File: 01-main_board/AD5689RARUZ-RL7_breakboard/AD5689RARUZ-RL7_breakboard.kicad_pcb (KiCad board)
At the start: 2 copper layers, 37.5 x 24 mm, 7 parts, among them J1 Conn_01x06, J2 Conn_01x08, U1 AD5689RARUZ-RL7

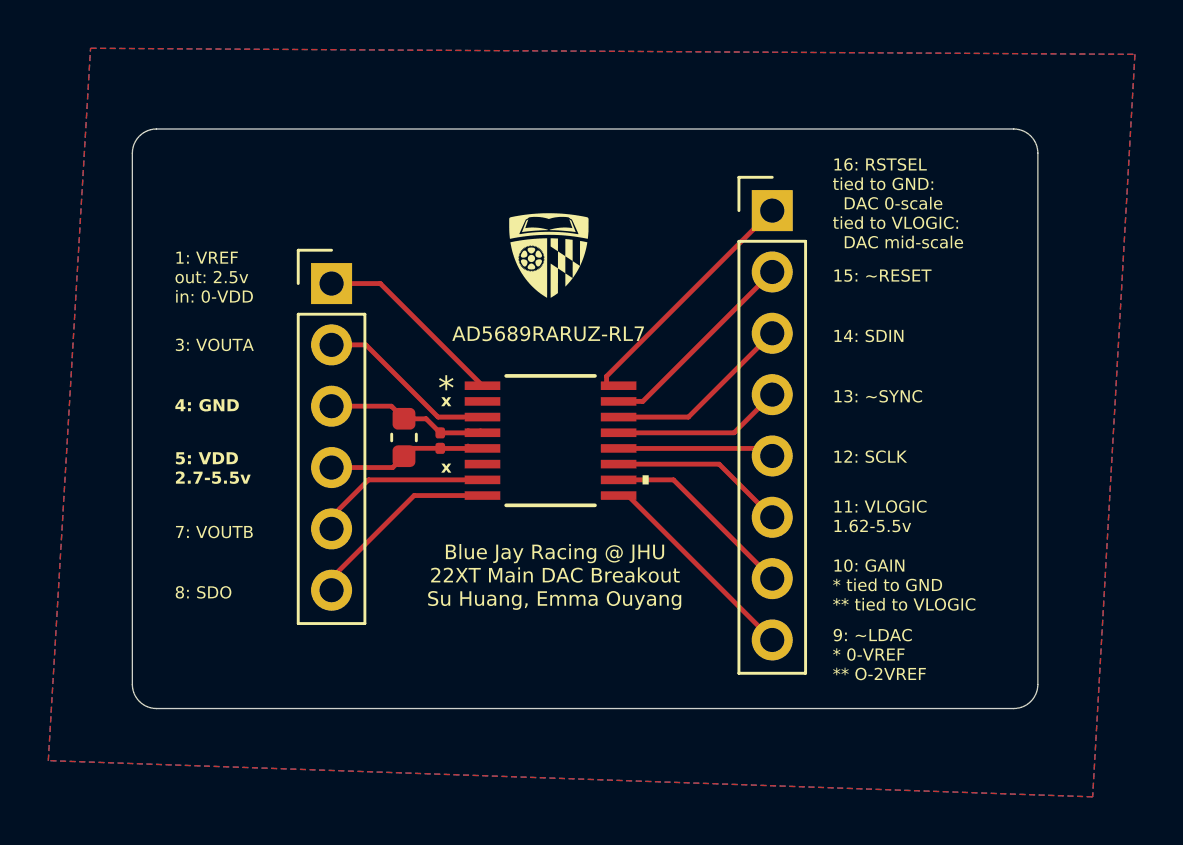
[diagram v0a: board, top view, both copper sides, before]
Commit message: updated breakout size
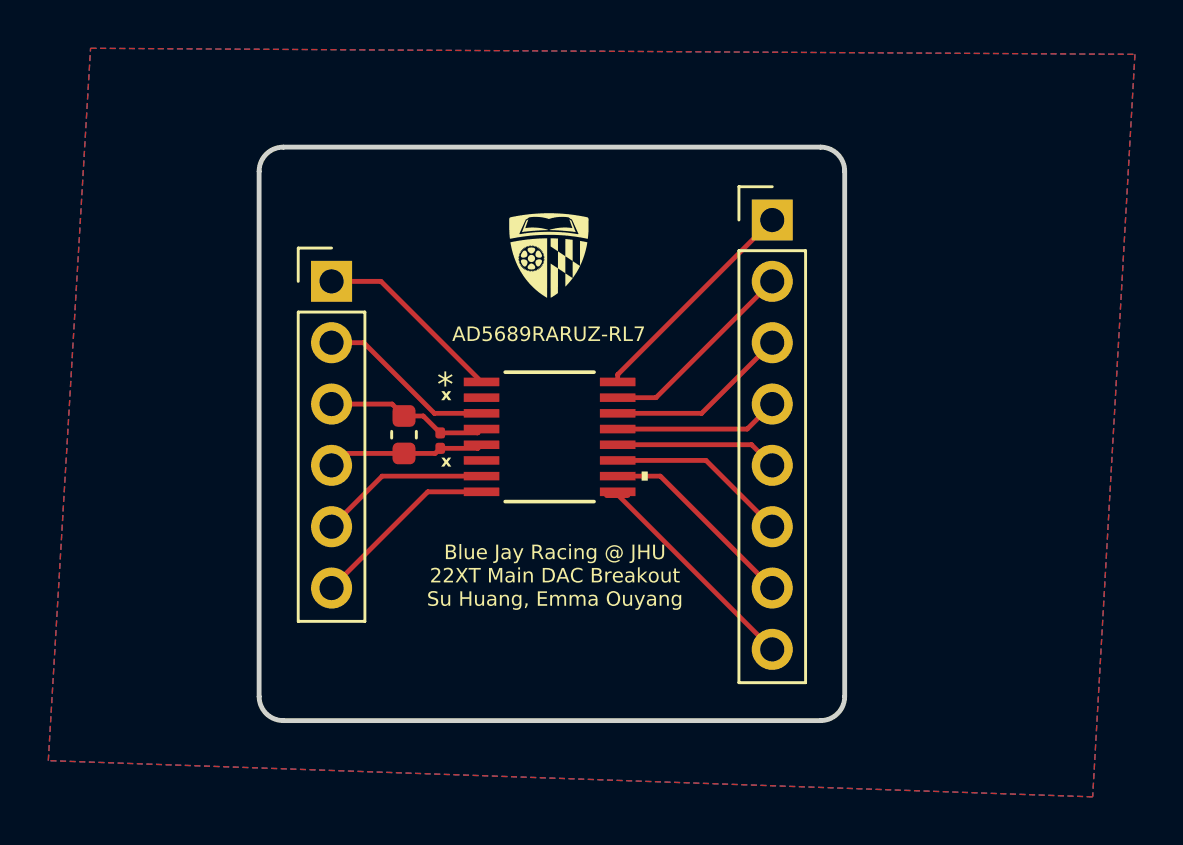
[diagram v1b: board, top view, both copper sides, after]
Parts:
- removed the G*** at (144.8, 66.2)
- moved J2 0.39 mm to (154.0, 64.8)
- moved U1 0.16 mm to (144.8, 73.8)
- moved C1 0.12 mm to (138.8, 73.7)
- moved J1 0.09 mm to (135.8, 67.3)
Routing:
- net RSTSEL: track 10.1 -> 9.36 mm
- net *LDAC: track 9.34 -> 10.1 mm
- net GND: track 7.46 -> 6.77 mm
- net SDIN: track 8.30 -> 7.61 mm
- net *RESET: track 9.08 -> 8.40 mm
- net *SYNC: track 7.52 -> 6.83 mm
- net VOUTA: track 7.99 -> 7.42 mm
- net VREF: track 8.50 -> 7.94 mm
- net VOUTB: track 7.59 -> 7.08 mm
- net SDO: track 8.37 -> 7.86 mm
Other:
- board size 37.5 x 24 mm -> 24.2 x 23.8 mm

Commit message: Checked and added via stitching
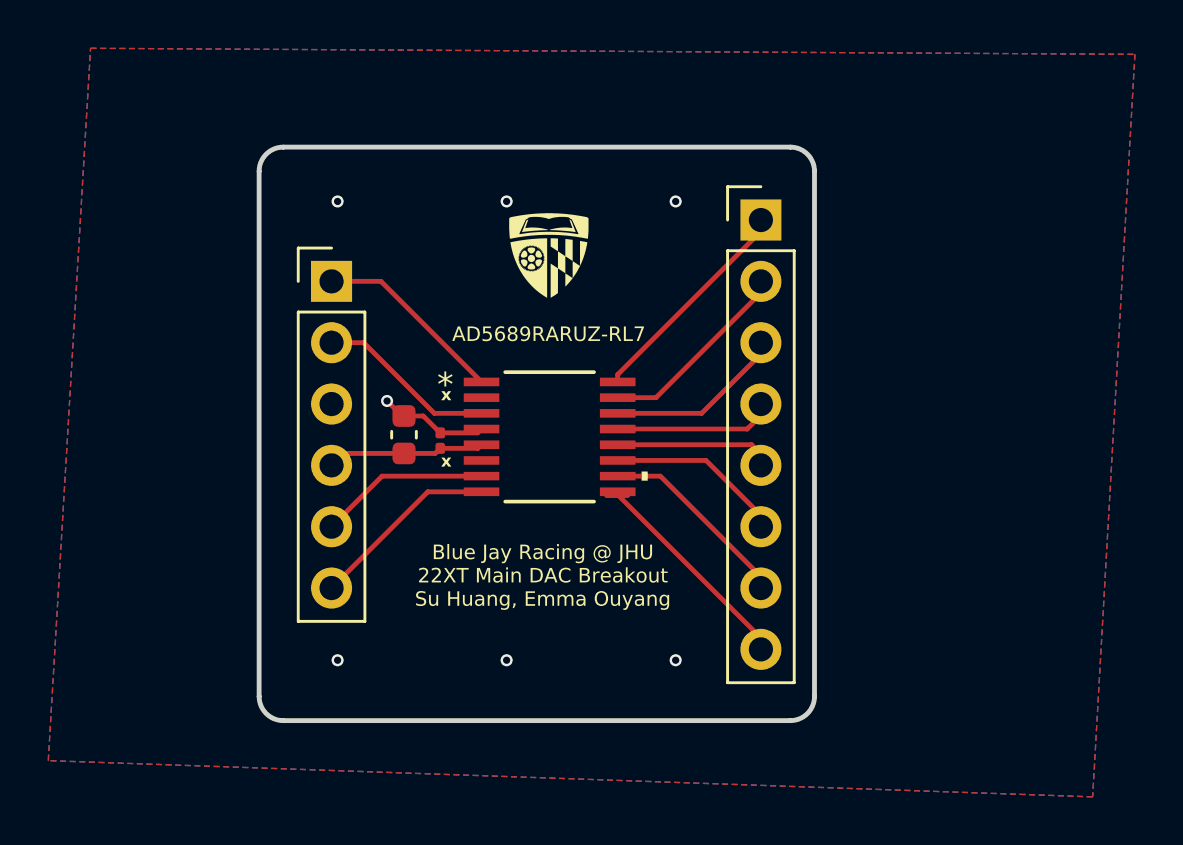
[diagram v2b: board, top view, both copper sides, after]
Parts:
- moved J2 0.47 mm to (153.5, 64.8)
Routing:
- net GND: track 6.77 -> 4.53 mm, vias 0 -> 7
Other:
- board size 24.2 x 23.8 mm -> 23 x 23.8 mm
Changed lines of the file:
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@@
 			(sketchdnponfab yes)
 			(crossoutdnponfab yes)
-			(subtractmaskfromsilk no)
+			(subtractmaskfromsilk yes)
 			(outputformat 1)
 			(mirror no)
@@
 	(footprint "Connector_PinHeader_2.54mm:PinHeader_1x08_P2.54mm_Vertical"
 		(layer "F.Cu")
-		(at 154 64.77)
+		(at 153.53 64.77)
 		(descr "Through hole straight pin header, 1x08, 2.54mm pitch, single row")
 		(tags "Through hole pin header THT 1x08 2.54mm single row")
@@
 		(model "${KICAD9_3DMODEL_DIR}/Connector_PinHeader_2.54mm.3dshapes/PinHeader_1x08_P2.54mm_Vertical.step"
 			(offset
-				(xyz 0 0 0)
+				(xyz 0 0 -1.5)
 			)
 			(scale
@@
 		(model "${KICAD9_3DMODEL_DIR}/Connector_PinHeader_2.54mm.3dshapes/PinHeader_1x06_P2.54mm_Vertical.step"
 			(offset
-				(xyz 0 0 0)
+				(xyz 0 0 -1.5)
 			)
 			(scale
@@
 	)
 	(gr_arc
-		(start 157 84.5)
-		(mid 156.707107 85.207107)
-		(end 156 85.5)
+		(start 155.75 84.5)
+		(mid 155.457107 85.207107)
+		(end 154.75 85.5)
 		(stroke
 			(width 0.2)
@@
 	)
 	(gr_line
-		(start 157 62.75)
-		(end 157 84.5)
+		(start 155.75 62.75)
+		(end 155.75 84.5)
 		(stroke
 			(width 0.2)
@@
 	(gr_line
 		(start 133.75 61.75)
-		(end 156 61.75)
+		(end 154.75 61.75)
 		(stroke
 			(width 0.2)
-			(type default)
+			(type solid)
 		)
 		(layer "Edge.Cuts")
 	)
 	(gr_line
-		(start 156 85.5)
-		(end 133.75 85.5)
+		(start 133.75 85.5)
+		(end 154.75 85.5)
 		(stroke
 			(width 0.2)
-			(type default)
+			(type solid)
 		)
 		(layer "Edge.Cuts")
 	)
 	(gr_arc
-		(start 156 61.75)
-		(mid 156.707107 62.042893)
-		(end 157 62.75)
+		(start 154.75 61.75)
+		(mid 155.457107 62.042893)
+		(end 155.75 62.75)
 		(stroke
 			(width 0.2)
@@
 	)
 	(gr_text "Blue Jay Racing @ JHU\n22XT Main DAC Breakout\nSu Huang, Emma Ouyang"
-		(at 145 79.5 0)
+		(at 144.5 79.5 0)
 		(layer "F.SilkS")
 		(effects
@@
 		)
 	)
+	(dimension
+		(type orthogonal)
+		(layer "Cmts.User")
+		(pts
+			(xy 135.75 81.28) (xy 153.543 81.28)
+		)
+		(height 11.303)
+		(orientation 0)
+		(format
+			(prefix "")
+			(suffix "")
+			(units 0)
+			(units_format 0)
+			(precision 4)
+			(suppress_zeroes yes)
+		)
+		(style
+			(thickness 0.2)
+			(arrow_length 1.27)
+			(text_position_mode 0)
+			(arrow_direction outward)
+			(extension_height 0.58642)
+			(extension_offset 0.5)
+			(keep_text_aligned yes)
+		)
+		(gr_text "0.7005"
+			(at 144.6465 90.783 0)
+			(layer "Cmts.User")
+			(effects
+				(font
+					(size 1.5 1.5)
+					(thickness 0.3)
+				)
+			)
+		)
+	)
 	(segment
 		(start 139.55 72.885)
@@
 	)
 	(segment
-		(start 135.75 72.39)
-		(end 138.255 72.39)
+		(start 138.75 72.885)
+		(end 138.671 72.885)
 		(width 0.2)
 		(layer "F.Cu")
@@
 	)
 	(segment
-		(start 138.255 72.39)
-		(end 138.75 72.885)
+		(start 138.671 72.885)
+		(end 138.049 72.263)
 		(width 0.2)
 		(layer "F.Cu")
@@
 		(net 1)
 	)
+	(via
+		(at 136 83)
+		(size 0.5)
+		(drill 0.3)
+		(layers "F.Cu" "B.Cu")
+		(net 1)
+	)
+	(via
+		(at 143 83)
+		(size 0.5)
+		(drill 0.3)
+		(layers "F.Cu" "B.Cu")
+		(net 1)
+	)
+	(via
+		(at 143 64)
+		(size 0.5)
+		(drill 0.3)
+		(layers "F.Cu" "B.Cu")
+		(net 1)
+	)
+	(via
+		(at 136 64)
+		(size 0.5)
+		(drill 0.3)
+		(layers "F.Cu" "B.Cu")
+		(net 1)
+	)
+	(via
+		(at 138.049 72.263)
+		(size 0.5)
+		(drill 0.3)
+		(layers "F.Cu" "B.Cu")
+		(net 1)
+	)
+	(via
+		(at 150 83)
+		(size 0.5)
+		(drill 0.3)
+		(layers "F.Cu" "B.Cu")
+		(net 1)
+	)
+	(via
+		(at 150 64)
+		(size 0.5)
+		(drill 0.3)
+		(layers "F.Cu" "B.Cu")
+		(net 1)
+	)
 	(segment
 		(start 140.25 74.225)
@@
 	)
 	(zone
+		(net 0)
+		(net_name "")
+		(layer "F.Cu")
+		(name "Keepout")
+		(hatch edge 0.5)
+		(connect_pads
+			(clearance 0)
+		)
+		(min_thickness 0.25)
+		(filled_areas_thickness no)
+		(keepout
+			(tracks allowed)
+			(vias allowed)
+			(pads allowed)
+			(copperpour not_allowed)
+			(footprints allowed)
+		)
+		(placement
+			(enabled no)
+			(sheetname "")
+		)
+		(fill
+			(thermal_gap 0.5)
+			(thermal_bridge_width 0.5)
+		)
+		(polygon
+			(pts
+				(xy 139.319 74.549) (xy 140.966539 74.549) (xy 140.966539 75.184) (xy 139.192 75.184) (xy 139.192 74.672185)
+				(xy 139.319 74.545185)
+			)
+		)
+	)
+	(zone

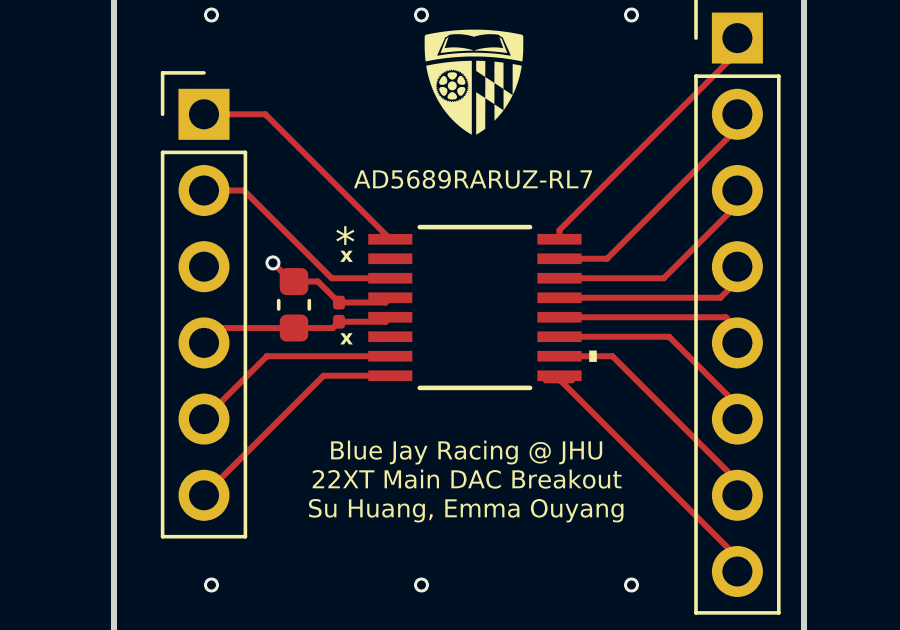
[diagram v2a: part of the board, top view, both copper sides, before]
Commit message: changed 0201 to 0402 capacitor
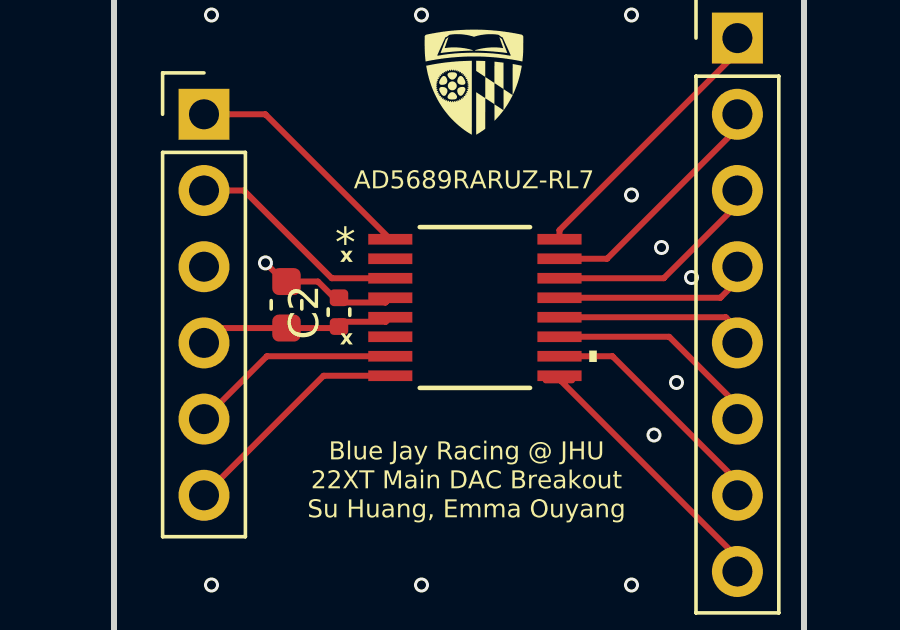
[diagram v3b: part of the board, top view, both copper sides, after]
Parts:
- C2: footprint Capacitor_SMD:C_0201_0603Metric -> Capacitor_SMD:C_0402_1005Metric
- moved C1 0.25 mm to (138.5, 73.7)
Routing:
- net GND: track 4.53 -> 5.17 mm, vias 7 -> 12
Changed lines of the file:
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@@
 	(footprint "Capacitor_SMD:C_0603_1608Metric"
 		(layer "F.Cu")
-		(at 138.75 73.66 90)
+		(at 138.5 73.66 90)
 		(descr "Capacitor SMD 0603 (1608 Metric), square (rectangular) end terminal, IPC-7351 nominal, (Body size source: IPC-SM-782 page 76, https://www.pcb-3d.com/wordpress/wp-content/uploads/ipc-sm-782a_amendment_1_and_2.pdf), generated with kicad-footprint-generator")
 		(tags "capacitor")
@@
 		)
 	)
-	(footprint "Capacitor_SMD:C_0201_0603Metric"
+	(footprint "Capacitor_SMD:C_0402_1005Metric"
 		(layer "F.Cu")
 		(at 140.25 73.905 90)
-		(descr "Capacitor SMD 0201 (0603 Metric), square (rectangular) end terminal, IPC-7351 nominal, (Body size source: https://www.vishay.com/docs/20052/crcw0201e3.pdf), generated with kicad-footprint-generator")
+		(descr "Capacitor SMD 0402 (1005 Metric), square (rectangular) end terminal, IPC-7351 nominal, (Body size source: IPC-SM-782 page 76, https://www.pcb-3d.com/wordpress/wp-content/uploads/ipc-sm-782a_amendment_1_and_2.pdf), generated with kicad-footprint-generator")
 		(tags "capacitor")
 		(property "Reference" "C2"
-			(at -1.345 0 180)
+			(at 0 -1.16 90)
 			(layer "F.SilkS")
-			(hide yes)
 			(effects
 				(font
-					(size 0.6 0.6)
-					(thickness 0.125)
-					(bold yes)
+					(size 1 1)
+					(thickness 0.15)
 				)
 			)
 		)
 		(property "Value" "0.1 μF"
-			(at 0 1.05 90)
+			(at 0 1.16 90)
 			(layer "F.Fab")
-			(hide yes)
 			(effects
 				(font
@@
 			)
 		)
-		(property "Datasheet" "~"
+		(property "Datasheet" ""
 			(at 0 0 90)
 			(layer "F.Fab")
@@
 			)
 		)
-		(property "Description" "Unpolarized capacitor"
+		(property "Description" ""
 			(at 0 0 90)
 			(layer "F.Fab")
@@
 		(attr smd)
 		(fp_line
-			(start 0.7 -0.35)
-			(end 0.7 0.35)
+			(start -0.107836 -0.36)
+			(end 0.107836 -0.36)
+			(stroke
+				(width 0.12)
+				(type solid)
+			)
+			(layer "F.SilkS")
+		)
+		(fp_line
+			(start -0.107836 0.36)
+			(end 0.107836 0.36)
+			(stroke
+				(width 0.12)
+				(type solid)
+			)
+			(layer "F.SilkS")
+		)
+		(fp_line
+			(start 0.91 -0.46)
+			(end 0.91 0.46)
 			(stroke
 				(width 0.05)
@@
 		)
 		(fp_line
-			(start -0.7 -0.35)
-			(end 0.7 -0.35)
+			(start -0.91 -0.46)
+			(end 0.91 -0.46)
 			(stroke
 				(width 0.05)
@@
 		)
 		(fp_line
-			(start 0.7 0.35)
-			(end -0.7 0.35)
+			(start 0.91 0.46)
+			(end -0.91 0.46)
 			(stroke
 				(width 0.05)
@@
 		)
 		(fp_line
-			(start -0.7 0.35)
-			(end -0.7 -0.35)
+			(start -0.91 0.46)
+			(end -0.91 -0.46)
 			(stroke
 				(width 0.05)
@@
 		)
 		(fp_line
-			(start 0.3 -0.15)
-			(end 0.3 0.15)
+			(start 0.5 -0.25)
+			(end 0.5 0.25)
 			(stroke
 				(width 0.1)
@@
 		)
 		(fp_line
-			(start -0.3 -0.15)
-			(end 0.3 -0.15)
+			(start -0.5 -0.25)
+			(end 0.5 -0.25)
 			(stroke
 				(width 0.1)
@@
 		)
 		(fp_line
-			(start 0.3 0.15)
-			(end -0.3 0.15)
+			(start 0.5 0.25)
+			(end -0.5 0.25)
 			(stroke
 				(width 0.1)
@@
 		)
 		(fp_line
-			(start -0.3 0.15)
-			(end -0.3 -0.15)
+			(start -0.5 0.25)
+			(end -0.5 -0.25)
 			(stroke
 				(width 0.1)
@@
 			(layer "F.Fab")
 		)
-		(pad "" smd roundrect
-			(at -0.345 0 90)
-			(size 0.318 0.36)
-			(layers "F.Paste")
-			(roundrect_rratio 0.25)
-		)
-		(pad "" smd roundrect
-			(at 0.345 0 90)
-			(size 0.318 0.36)
-			(layers "F.Paste")
-			(roundrect_rratio 0.25)
+		(fp_text user "${REFERENCE}"
+			(at 0 0 90)
+			(layer "F.Fab")
+			(effects
+				(font
+					(size 0.25 0.25)
+					(thickness 0.04)
+				)
+			)
 		)
 		(pad "1" smd roundrect
-			(at -0.32 0 90)
-			(size 0.46 0.4)
-			(layers "F.Cu" "F.Mask")
+			(at -0.48 0 90)
+			(size 0.56 0.62)
+			(layers "F.Cu" "F.Mask" "F.Paste")
 			(roundrect_rratio 0.25)
 			(net 2 "VDD")
@@
 		)
 		(pad "2" smd roundrect
-			(at 0.32 0 90)
-			(size 0.46 0.4)
-			(layers "F.Cu" "F.Mask")
+			(at 0.48 0 90)
+			(size 0.56 0.62)
+			(layers "F.Cu" "F.Mask" "F.Paste")
 			(roundrect_rratio 0.25)
 			(net 1 "GND")
@@
 		)
 		(embedded_fonts no)
-		(model "${KICAD9_3DMODEL_DIR}/Capacitor_SMD.3dshapes/C_0201_0603Metric.step"
+		(model "${KICAD9_3DMODEL_DIR}/Capacitor_SMD.3dshapes/C_0402_1005Metric.step"
 			(offset
 				(xyz 0 0 0)
@@
 	)
 	(segment
-		(start 139.55 72.885)
+		(start 141.800599 73.585)
 		(end 140.25 73.585)
 		(width 0.2)
@@
 	)
 	(segment
-		(start 141.800599 73.585)
-		(end 141.9606 73.424999)
+		(start 139.55 72.885)
+		(end 138.5 72.885)
 		(width 0.2)
 		(layer "F.Cu")
@@
 	)
 	(segment
-		(start 138.75 72.885)
-		(end 139.55 72.885)
+		(start 135.75 72.39)
+		(end 136.14 72.39)
+		(width 0.2)
+		(layer "F.Cu")
+		(net 1)
+	)
+	(segment
+		(start 141.9606 73.424999)
+		(end 141.800599 73.585)
 		(width 0.2)
 		(layer "F.Cu")
@@
 	)
 	(segment
-		(start 138.671 72.885)
-		(end 138.049 72.263)
+		(start 138.421 72.885)
+		(end 137.799 72.263)
 		(width 0.2)
 		(layer "F.Cu")
@@
 	(segment
 		(start 140.25 73.585)
-		(end 141.800599 73.585)
+		(end 139.55 72.885)
 		(width 0.2)
 		(layer "F.Cu")
@@
 	)
 	(via
+		(at 151 71.75)
+		(size 0.5)
+		(drill 0.3)
+		(layers "F.Cu" "B.Cu")
+		(net 1)
+	)
+	(via
 		(at 136 83)
 		(size 0.5)
@@
 	)
 	(via
-		(at 138.049 72.263)
+		(at 150.75 78)
+		(size 0.5)
+		(drill 0.3)
+		(layers "F.Cu" "B.Cu")
+		(net 1)
+	)
+	(via
+		(at 151.5 76.25)
+		(size 0.5)
+		(drill 0.3)
+		(layers "F.Cu" "B.Cu")
+		(net 1)
+	)
+	(via
+		(at 137.799 72.263)
+		(size 0.5)
+		(drill 0.3)
+		(layers "F.Cu" "B.Cu")
+		(net 1)
+	)
+	(via
+		(at 152 72.75)
 		(size 0.5)
 		(drill 0.3)
@@
 		(net 1)
 	)
+	(via
+		(at 150 70)
+		(size 0.5)
+		(drill 0.3)
+		(layers "F.Cu" "B.Cu")
+		(net 1)
+	)
 	(segment
 		(start 140.25 74.225)
@@
 	)
 	(segment
-		(start 139.075 74.225)
-		(end 138.75 74.55)
-		(width 0.2)
-		(layer "F.Cu")
-		(net 2)
-	)
-	(segment
 		(start 138.75 74.435)
 		(end 140.04 74.435)
@@
 		(net_name "")
 		(layer "F.Cu")
-		(name "Keepout")
 		(hatch edge 0.5)
 		(connect_pads
@@
 		(polygon
 			(pts
-				(xy 139.319 74.549) (xy 140.966539 74.549) (xy 140.966539 75.184) (xy 139.192 75.184) (xy 139.192 74.672185)
-				(xy 139.319 74.545185)
+				(xy 151.5 74.25) (xy 152.75 74.25) (xy 152.75 75.5) (xy 151.5 75.5)
+			)
+		)
+	)
+	(zone
+		(net 0)
+		(net_name "")
+		(layer "F.Cu")
+		(hatch edge 0.5)
+		(connect_pads yes
+			(clearance 0)
+		)
+		(min_thickness 0.25)
+		(filled_areas_thickness no)
+		(keepout
+			(tracks allowed)
+			(vias allowed)
+			(pads allowed)
+			(copperpour not_allowed)
+			(footprints allowed)
+		)
+		(placement
+			(enabled no)
+			(sheetname "")
+		)
+		(fill
+			(thermal_gap 0.5)
+			(thermal_bridge_width 0.5)
+			(island_removal_mode 1)
+			(island_area_min 10)
+		)
+		(polygon
+			(pts
+				(xy 141.25 74.5) (xy 141.25 75.25) (xy 138.5 75.25) (xy 138.5 74.5)
 			)
 		)
